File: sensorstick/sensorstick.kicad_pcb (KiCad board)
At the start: 2 copper layers, 85 x 23 mm, 8 parts, among them J1 U217-04XN-XXR84, U1 ESP32-C3_SUPERMINI, U2 SCD40 CO2 module

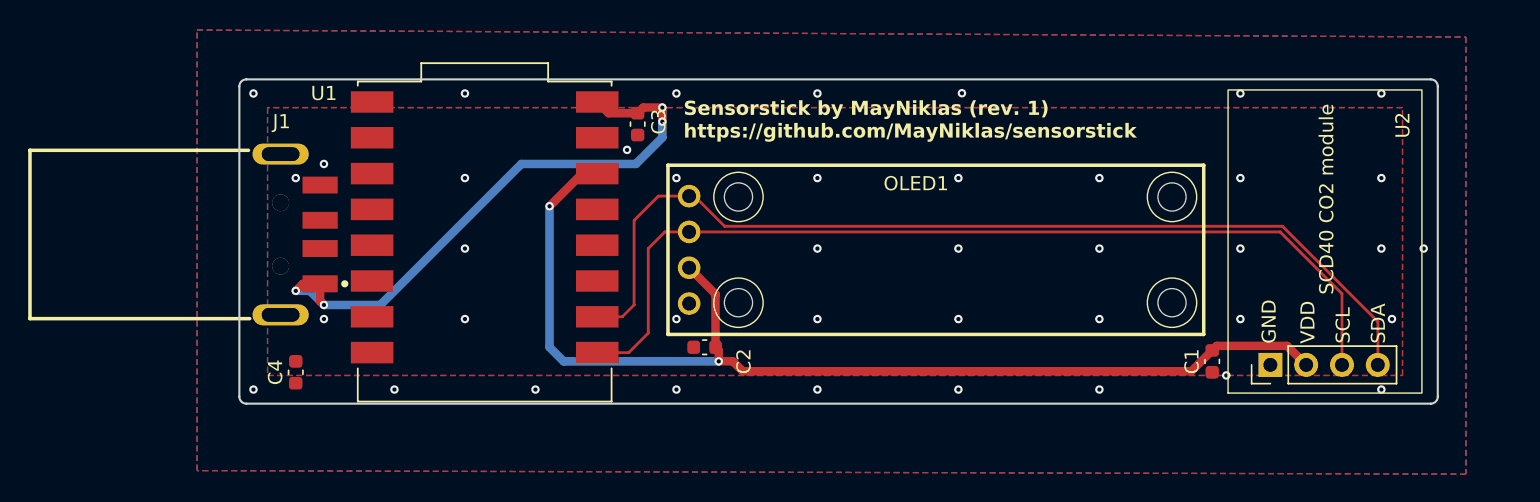
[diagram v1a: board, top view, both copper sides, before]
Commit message: new sensor possition
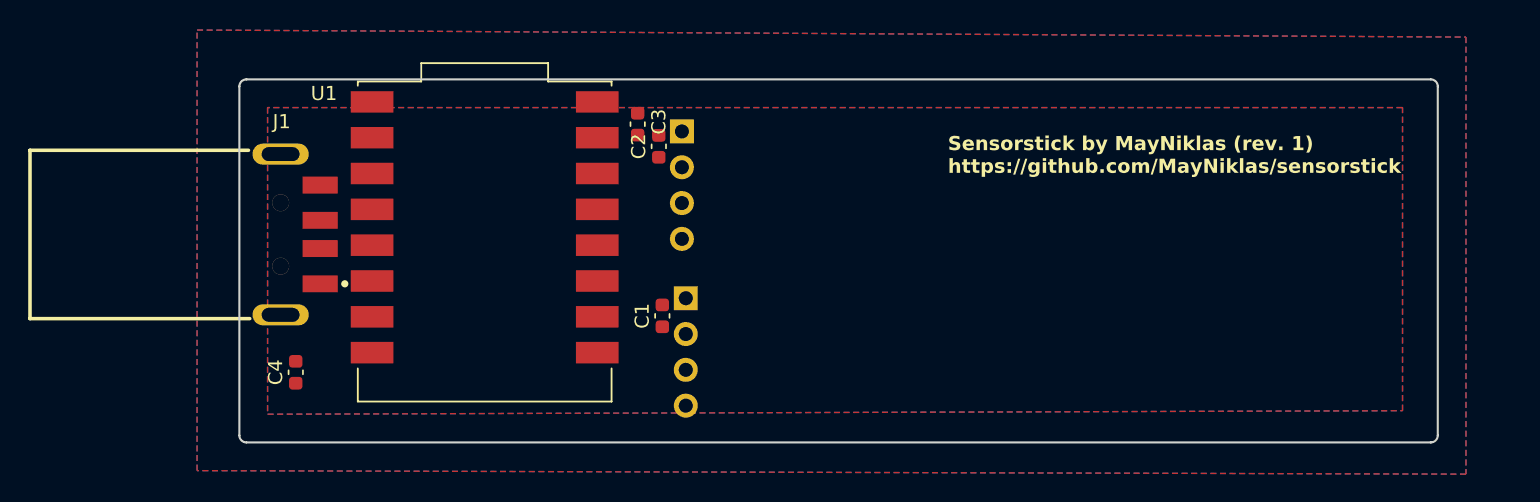
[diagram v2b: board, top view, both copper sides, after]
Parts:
- removed OLED1: HS91L02W2C01, CustomLibrary:OLED-TH_L38.0-W12.0_HS91L02W2C01
- added U3: GY-SGP30, CustomLibrary:GY-SGP30_VOC_module, B.Cu at (93.2, 101.4)
- U2: moved to B.Cu
- moved U2 45.1 mm to (91.4, 90.6), turned to 180 degrees
- moved C1 39.1 mm to (90.0, 104.3)
- moved C2 14.6 mm to (89.8, 92.2), turned to 90 degrees
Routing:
- net +3.3V: track 77.5 -> 0.00 mm, vias 2 -> 0
- net /IC2_SDA: track 69.2 -> 0.00 mm
- net /I2C_SCL: track 66.7 -> 0.00 mm
- net +5V: track 43.1 -> 0.00 mm, vias 4 -> 0
- net GND: vias 25 -> 0
- net Earth: vias 16 -> 0
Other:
- board size 85 x 23 mm -> 85 x 25.8 mm

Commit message: added traceing
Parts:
- moved C4 3.20 mm to (64.0, 111.5)
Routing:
- net +5V: track 0.00 -> 31.9 mm
- net /IC2_SDA: track 0.00 -> 23.3 mm, vias 0 -> 1
- net /I2C_SCL: track 0.00 -> 20.1 mm
- net +3.3V: track 0.00 -> 18.6 mm
- net GND: track 0.00 -> 11.2 mm, vias 0 -> 17
- net Earth: vias 0 -> 20
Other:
- board size 85 x 25.8 mm -> 35.8 x 25.8 mm

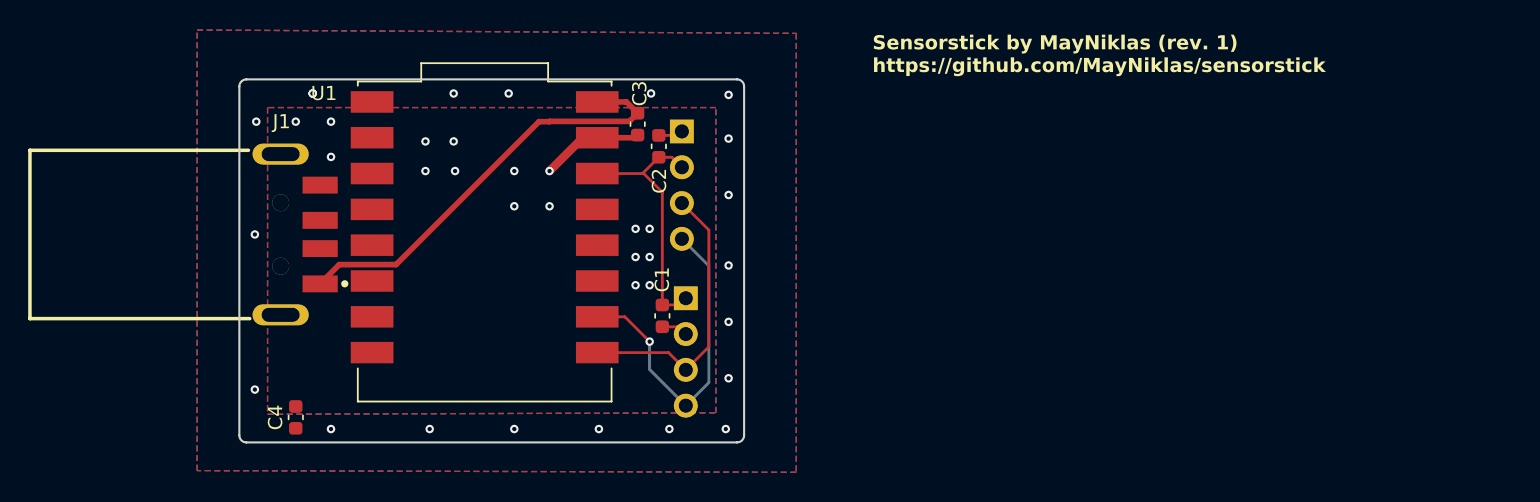
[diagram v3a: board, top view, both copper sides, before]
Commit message: changed esp possition
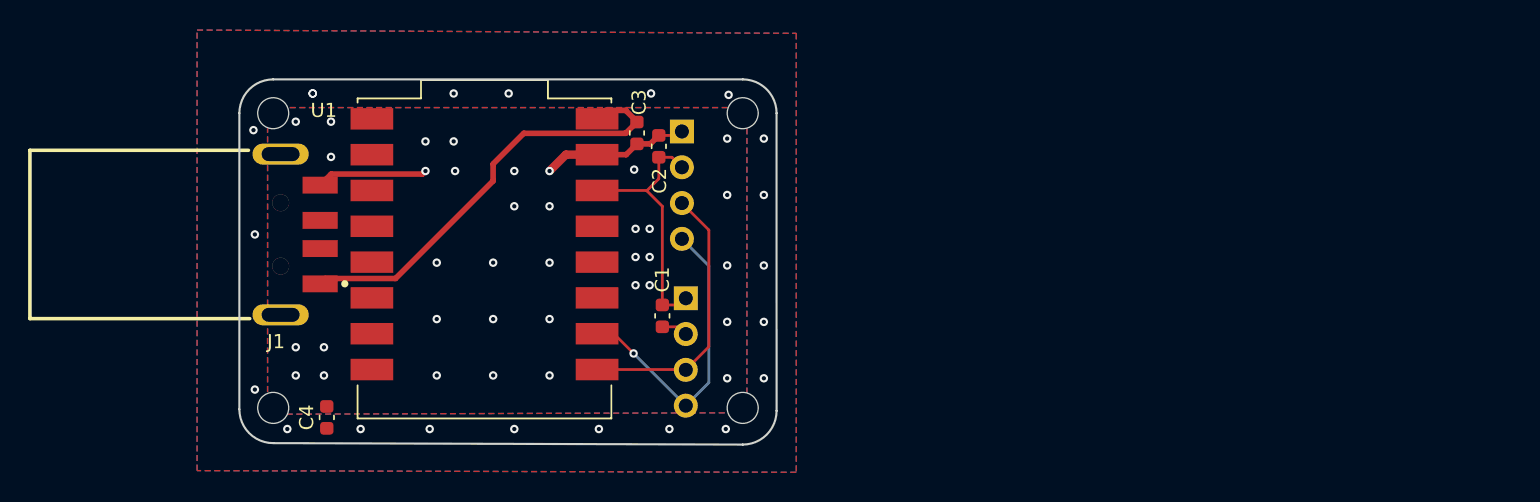
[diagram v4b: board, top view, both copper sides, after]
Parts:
- added REF**: MountingHole_2.2mm_M2, MountingHole:MountingHole_2.2mm_M2, F.Cu at (95.7, 89.9)
- added REF**: MountingHole_2.2mm_M2, MountingHole:MountingHole_2.2mm_M2, F.Cu at (62.4, 89.9)
- added REF**: MountingHole_2.2mm_M2, MountingHole:MountingHole_2.2mm_M2, F.Cu at (62.4, 110.8)
- added REF**: MountingHole_2.2mm_M2, MountingHole:MountingHole_2.2mm_M2, F.Cu at (95.7, 110.8)
- moved C4 2.20 mm to (66.2, 111.5)
- moved U1 1.20 mm to (77.4, 100.2)
- moved C3 0.63 mm to (88.2, 91.3)
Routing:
- net GND: track 11.2 -> 20.3 mm, vias 17 -> 36
- net /IC2_SDA: track 23.3 -> 21.7 mm
- net +5V: track 31.9 -> 31.4 mm
- net Earth: vias 20 -> 21
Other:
- board size 35.8 x 25.8 mm -> 38.1 x 25.9 mm

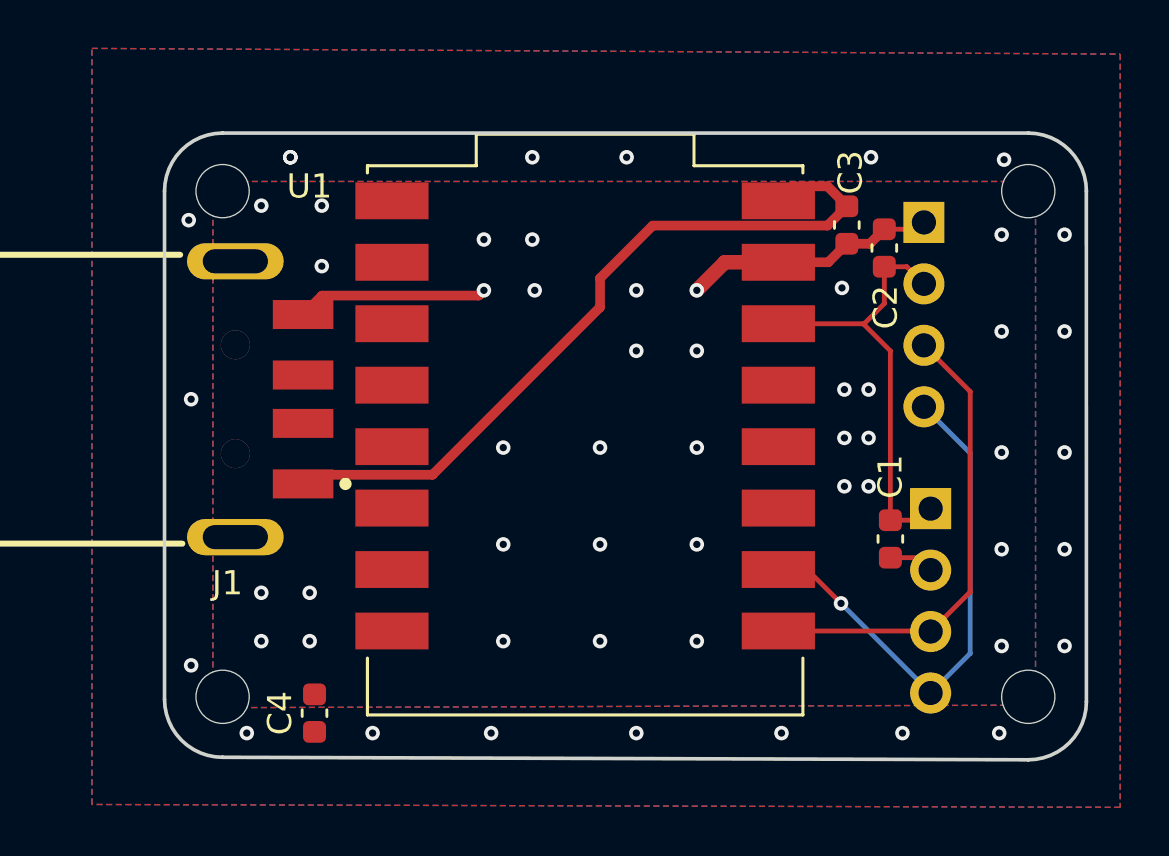
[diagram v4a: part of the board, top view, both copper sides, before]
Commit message: minimal desin with new sensor
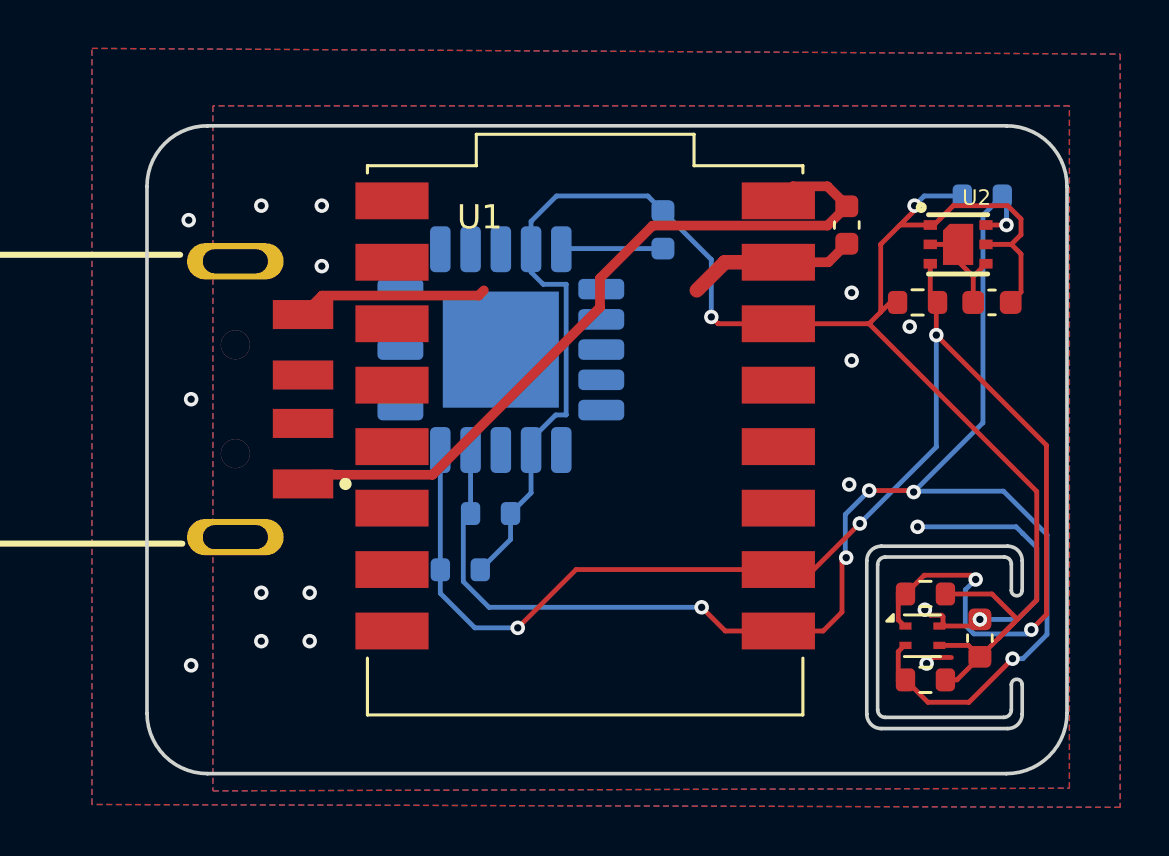
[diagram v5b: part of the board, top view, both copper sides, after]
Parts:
- removed C4: 100nF, Capacitor_SMD:C_0603_1608Metric
- removed REF** (x4): MountingHole_2.2mm_M2, MountingHole:MountingHole_2.2mm_M2
- added C5: 100nF, Capacitor_SMD:C_0603_1608Metric, F.Cu at (93.7, 108.4)
- added R1: 10kΩ, Resistor_SMD:R_0603_1608Metric, F.Cu at (91.5, 106.5)
- added R2: 10kΩ, Resistor_SMD:R_0603_1608Metric, B.Cu at (73.5, 103.2)
- added R3: 10kΩ, Resistor_SMD:R_0603_1608Metric, F.Cu at (91.1, 94.5)
- added R4: 10kΩ, Resistor_SMD:R_0603_1608Metric, B.Cu at (93.8, 90.1)
- added R5: 10kΩ, Resistor_SMD:R_0603_1608Metric, F.Cu at (91.5, 110.1)
- added R6: 10kΩ, Resistor_SMD:R_0603_1608Metric, B.Cu at (72.2, 105.5)
- added U4: SCD40-D-R2, Sensor:Sensirion_SCD4x-1EP_10.1x10.1mm_P1.25mm_EP4.8x4.8mm, B.Cu at (73.9, 96.5)
- C2: moved to B.Cu
- U2: value SCD40 CO2 module -> SGP30; footprint CustomLibrary:SCD40_CO2_module -> SGP30:SGP30; moved to F.Cu
- U3: value GY-SGP30 -> SHT4x; footprint CustomLibrary:GY-SGP30_VOC_module -> Sensor_Humidity:Sensirion_DFN-4_1.5x1.5mm_P0.8mm_SHT4x_NoCentralPad; moved to F.Cu
- moved C1 10.6 mm to (94.2, 94.5), turned to 0 degrees
- moved C2 9.18 mm to (80.6, 91.5), turned to -90 degrees
- moved U3 7.14 mm to (91.3, 108.3), turned to 0 degrees
- moved U2 2.05 mm to (92.8, 92.1), turned to 0 degrees
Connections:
- U2 pad 1: GND -> +3.3V
- U2 pad 2: +3.3V -> GND
- U2 pad 3: /I2C_SCL -> /IC2_SDA
- U2 pad 4: /IC2_SDA -> GND
- U3 pad 1: +3.3V -> /IC2_SDA
- U3 pad 2: GND -> /I2C_SCL
- U3 pad 3: /I2C_SCL -> +3.3V
- U3 pad 4: /IC2_SDA -> GND
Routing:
- net +3.3V: track 18.6 -> 80.1 mm, vias 0 -> 2
- net /I2C_SCL: track 19.6 -> 65.7 mm, vias 0 -> 6
- net /IC2_SDA: track 21.7 -> 62.4 mm, vias 1 -> 5
- net GND: track 20.3 -> 38.0 mm, vias 36 -> 15
- net +5V: track 31.4 -> 30.8 mm
- net Earth: vias 21 -> 3
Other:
- board size 38.1 x 25.9 mm -> 38 x 26.8 mm

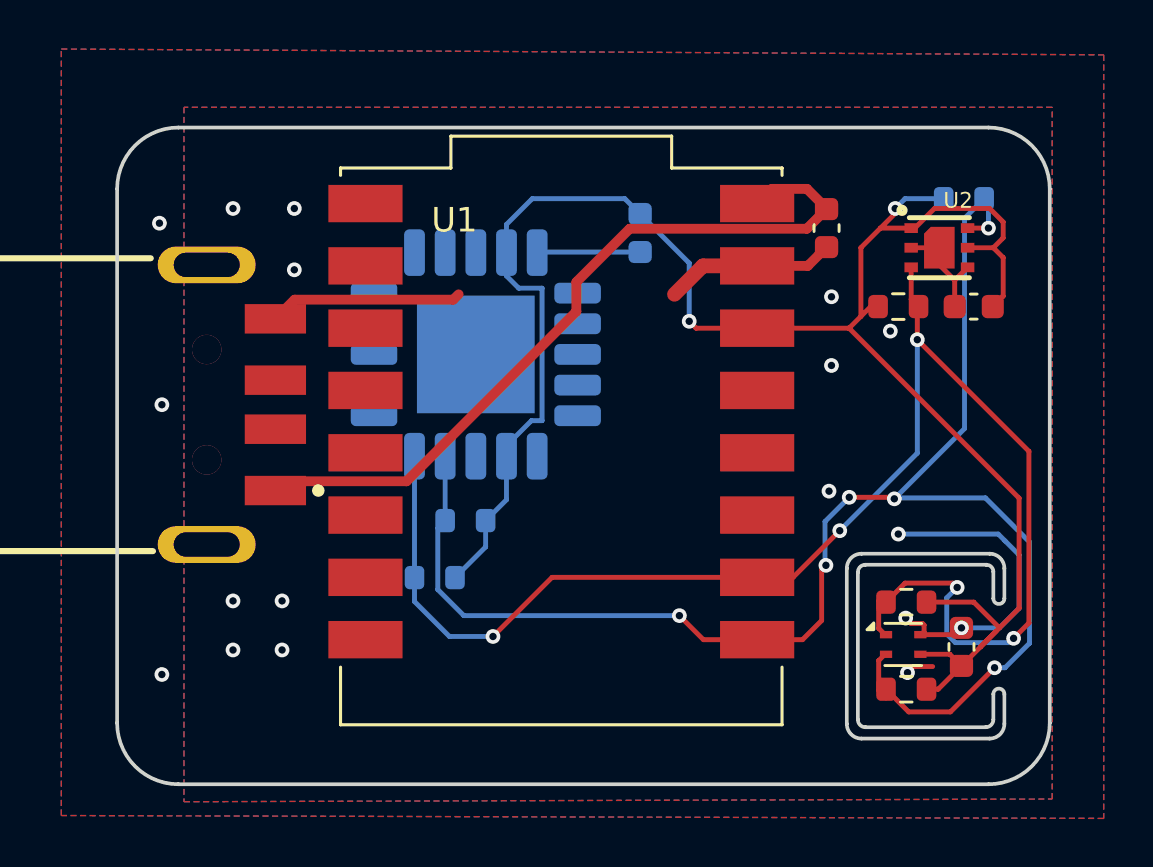
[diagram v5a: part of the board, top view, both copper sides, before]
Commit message: finished first routing, open for review
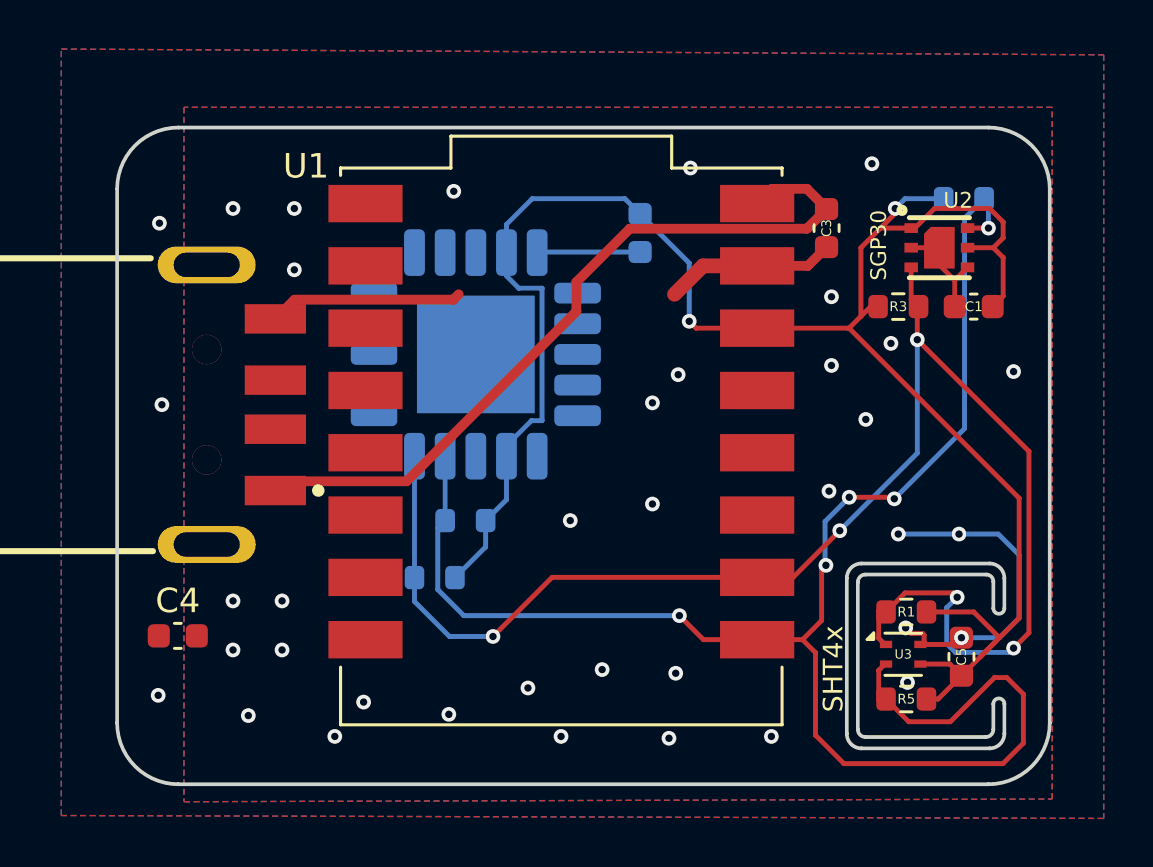
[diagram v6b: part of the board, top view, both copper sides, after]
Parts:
- added C4: 100nF, Capacitor_SMD:C_0603_1608Metric, F.Cu at (61.8, 107.9)
- U4: value SCD40-D-R2 -> SCD40
- moved C5 0.40 mm to (93.7, 108.8)
- moved R1 0.40 mm to (91.5, 107.0)
- moved R5 0.40 mm to (91.5, 110.5)
- moved U3 0.40 mm to (91.3, 108.7)
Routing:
- net /I2C_SCL: track 65.7 -> 70.2 mm, vias 6 -> 5
- net GND: track 38.0 -> 37.3 mm, vias 15 -> 35
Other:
- outline, holes or cut-outs redrawn
